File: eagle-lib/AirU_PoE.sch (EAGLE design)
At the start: 86 parts, among them Q1 BSS138W-7-F, Q2 MMBT3904LT1G, Q3 MMBT3904LT1G, Q5 NCE3407A, U1 HDC1080DMBT, U2 CH340T-SSOP20, U3 CJT1117-3.3-SOT223, U4 MAX2659-DFN6, U5 L70-M39, U6 MOLEX-53261-0871, U7 ESP32_WROOM32_SKINNY, U8 TLV2333, U9 MICS-4514, Y1 12MHZ

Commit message: Added PoE components
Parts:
- added C33: 10uf, Seeed-Capacitor:CERAMIC-10UF-10V-10%-X5R(0603)
- added C34, C35: 100nf, Seeed-Capacitor:CERAMIC-100NF-50V-10%-X7R(0603)
- added C36: 33nf, Seeed-Capacitor:CERAMIC-33NF-50V-10%-X7R(0603)
- added D10, D11, D12, D13, D14, D15, D16, D9: 250mA/100V, SparkFun-DiscreteSemi:DIODE-BAS16J
- added J8: SI-52003-F, SI-52003-F:SI-52003-F
- added L4: 330R-1500MA, Seeed-Inductor:SMD-FERRITE-BEAD-330R-1500MA(0805)'0805'
- added R39, R40: 470, SparkFun-Resistors:470OHM-0603-1/10W-1%
- added R41: 2.32k, SparkFun-Resistors:2.2KOHM-0603-1/10W-1%
- added R42, R43, R44, R45: 49.9, BeagleBone_Black_Wireless:R-US_M0805
- added R47: 1K, Seeed-Resistor:SMD-RES-1K-1%-1/10W(0603)
- added U$22: SPXO25MHZ7050-4P, 25MHZ_seeed:SPXO25MHZ7050-4P
- added U10: ENC28J60ENC28J60-I/SS0P, ENC28J60QFN:ENC28J60ENC28J60-I/SS0P
- added U13: AG9900M, AG9900M:AG9900M
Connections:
- removed net SD_CLK_IO14: R15.1, SD1.SCLK, U7.IO14/A2_6
- removed net SD_CMD_IO15: R17.1, SD1.DI, U7.IO15/A2_3
- removed net SD_CS_IO13: R8.1, SD1.CS, U7.IO13/A2_4
- removed net SD_D0_IO2: R12.2, R9.1, SD1.DO, U7.IO2/A2_2
- removed net SD_D1_IO4: SD1.DATA1, U7.IO4/A2_0
- removed net SD_D2_IO12: SD1.DATA2, U7.IO12/A2_5
- new net ETH_LED1: J8.C1, R39.2
- new net ETH_LED2: J8.C2, R40.2
- new net ETH_OSC1: U$22.OUT, U10.OSC1
- new net ETH_OSC2: R47.1, U10.OSC2
- new net ETH_TPIN+: J8.RD+, R43.2, U10.TPIN+
- new net ETH_TPIN-: J8.RD-, R42.1, U10.TPIN-
- new net ETH_TPOUT+: J8.TD+, R45.2, U10.TPOUT+
- new net ETH_TPOUT-: J8.TD-, R44.1, U10.TPOUT-
- new net ETH_VC1+: D10.C, D9.A, J8.VC1+
- new net ETH_VC1-: D15.A, D16.C, J8.VC1-
- new net ETH_VC2+: D11.C, D12.A, J8.VC2+
- new net ETH_VC2-: D13.A, D14.C, J8.VC2-
- new net LEDA: R39.1, U10.LEDA
- new net LEDB: R40.1, U10.LEDB
- new net N$43: C35.2, R42.2, R43.1
- new net N$46: C34.2, J8.CT, L4.1, R44.2, R45.1
- new net PHY_SPI_CS_IO16: U10.!CS, U7.IO16
- new net PHY_SPI_INT_IO25: U10.!INT, U7.IO25/DAC1/A2_8
- new net POE_VIN+: D12.C, D13.C, D15.C, D9.C, U13.VIN+@5, U13.VIN+@6
- new net POE_VIN-: D10.A, D11.A, D14.A, D16.A, U13.VIN-@7, U13.VIN-@8
- new net RBIAS: R41.1, U10.RBIAS
- new net SD_SPI_CS_IO5: R8.1, SD1.CS, U7.IO5
- new net SPI_CLK_IO14: R15.1, SD1.SCLK, U10.SCK, U7.IO14/A2_6
- new net SPI_MISO_IO12: R9.1, SD1.DO, U10.SO, U7.IO12/A2_5
- new net SPI_MOSI_IO15: R17.1, SD1.DI, U10.SI, U7.IO15/A2_3
- new net VCAP: C33.1, U10.VCAP
- net 3.3V: now also C36.1, J8.A1, J8.A2, L4.2, U$22.VCC, U10.VDD, U10.VDDOSC, U10.VDDPLL, U10.VDDRX, U10.VDDTX
- net 5.0V: now also U13.+VDC@1, U13.+VDC@2
- net GND: now also C33.2, C34.1, C35.1, C36.2, J8.S1, J8.S2, R41.2, R47.2, U$22.GND, U10.VSS, U10.VSSOSC, U10.VSSPLL, U10.VSSRX, U10.VSSTX, U13.-VDC
- net PM_RESET: now also R12.2, U7.IO2/A2_2; no longer U7.IO17
- net PM_SET: now also U7.IO4/A2_0; no longer U7.IO5
- net U2RXD: now also U7.IO13/A2_4; no longer U7.IO16
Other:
- note added: "Ethernet PHY"
- note added: "Oscillator (for Ethernet PHY)"
- note added: "Power Over Ethernet (PoE) control"
- note added: "RJ45 Ethernet Jack"

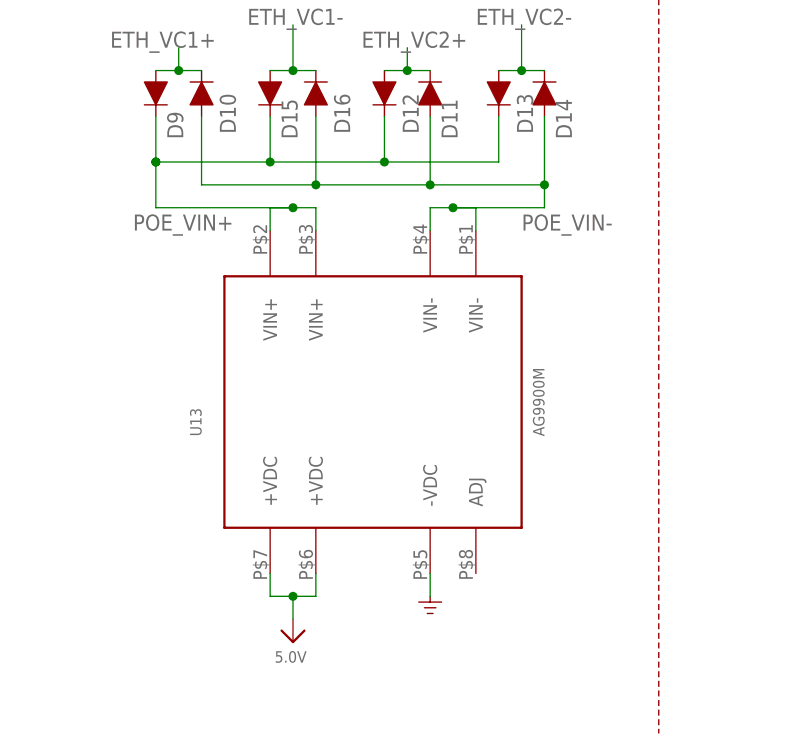
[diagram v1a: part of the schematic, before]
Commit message: fixed AG9900M pins
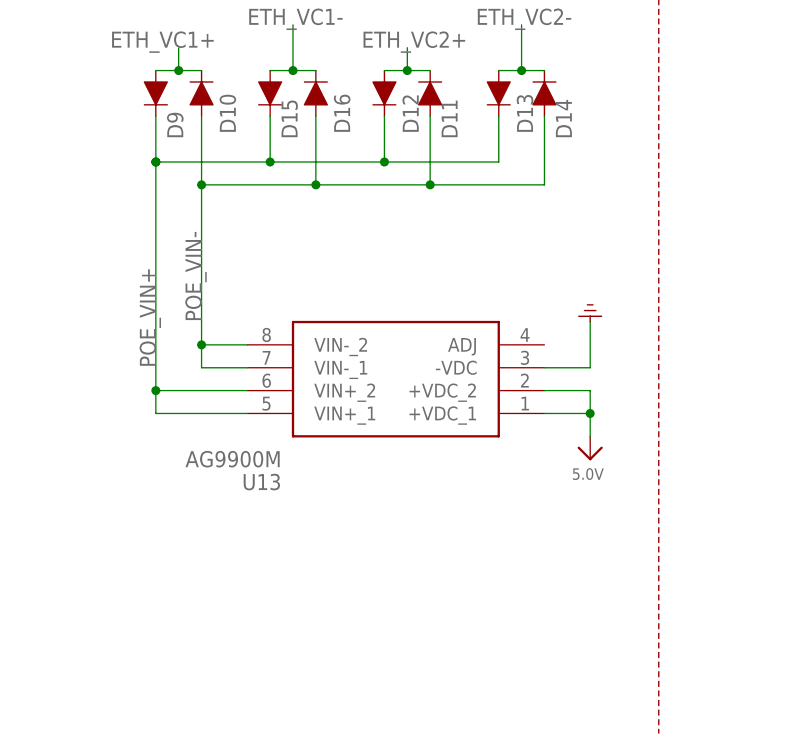
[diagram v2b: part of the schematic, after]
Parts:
- U13: device AG9900M:AG9900M -> Ag9900M:AG9900M
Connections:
- net 5.0V: now also U13.+VDC_1, U13.+VDC_2; no longer U13.+VDC@1, U13.+VDC@2
- net POE_VIN+: now also U13.VIN+_1, U13.VIN+_2; no longer U13.VIN+@5, U13.VIN+@6
- net POE_VIN-: now also U13.VIN-_1, U13.VIN-_2; no longer U13.VIN-@7, U13.VIN-@8
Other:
- moved on the sheet: U13
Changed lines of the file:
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@@
 <part name="U10" library="ENC28J60QFN" deviceset="ENC28J60" device="ENC28J60-I/SS0P" package3d_urn="urn:adsk.eagle:package:11158957/1"/>
 <part name="J8" library="SI-52003-F" deviceset="SI-52003-F" device=""/>
-<part name="U13" library="AG9900M" deviceset="AG9900M" device=""/>
 <part name="FRAME4" library="frames" library_urn="urn:adsk.eagle:library:229" deviceset="FRAME_B_L" device=""/>
 <part name="U$29" library="Power or GND " deviceset="GND_POWER" device=""/>
@@
 <part name="U$22" library="25MHZ_seeed" deviceset="SPXO25MHZ7050-4P" device="" package3d_urn="urn:adsk.eagle:package:14869334/1"/>
 <part name="C36" library="Seeed-Capacitor" deviceset="CERAMIC-33NF-50V-10%-X7R(0603)" device="" value="33nf"/>
+<part name="U13" library="Ag9900M" deviceset="AG9900M" device=""/>
 </parts>
 <sheets>
@@
 <attribute name="VALUE" x="259.065340625" y="55.8458" size="1.78141875" layer="96"/>
 </instance>
-<instance part="U13" gate="G$1" x="43.18" y="38.1" smashed="yes" rot="R90">
-<attribute name="NAME" x="25.4" y="33.02" size="1.27" layer="95" rot="R90"/>
-<attribute name="VALUE" x="63.5" y="33.02" size="1.27" layer="96" rot="R90"/>
-</instance>
 <instance part="FRAME4" gate="G$1" x="0" y="0" smashed="yes"/>
 <instance part="U$29" gate="G$1" x="299.72" y="68.58" smashed="yes" rot="R270"/>
@@
 <attribute name="VALUE" x="158.496" y="128.016" size="1.27" layer="96"/>
 </instance>
-<instance part="U$66" gate="G$1" x="50.8" y="15.24" smashed="yes"/>
+<instance part="U$66" gate="G$1" x="68.58" y="45.72" smashed="yes" rot="R180"/>
 <instance part="U$67" gate="G$1" x="168.91" y="45.72" smashed="yes" rot="R90"/>
 <instance part="U$68" gate="G$1" x="168.91" y="58.42" smashed="yes" rot="R90"/>
@@
 <attribute name="VALUE" x="103.124" y="72.136" size="1.27" layer="96" rot="R90"/>
 </instance>
-<instance part="U$94" gate="G$1" x="35.56" y="10.16" smashed="yes" rot="R180">
-<attribute name="VALUE" x="37.084" y="9.144" size="1.27" layer="96" rot="R180"/>
+<instance part="U$94" gate="G$1" x="68.58" y="30.48" smashed="yes" rot="R180">
+<attribute name="VALUE" x="70.104" y="29.464" size="1.27" layer="96" rot="R180"/>
 </instance>
 <instance part="U$1" gate="G$1" x="218.44" y="78.74" smashed="yes">
@@
 <attribute name="NAME" x="326.39" y="45.72" size="1.27" layer="95" ratio="10" rot="R180"/>
 <attribute name="VALUE" x="326.39" y="49.53" size="1.27" layer="96" ratio="10" rot="R180"/>
+</instance>
+<instance part="U13" gate="G$1" x="63.5" y="35.56" smashed="yes" rot="R180">
+<attribute name="NAME" x="34.29" y="27.94" size="1.778" layer="95" rot="R180" align="center-left"/>
+<attribute name="VALUE" x="34.29" y="30.48" size="1.778" layer="96" rot="R180" align="center-left"/>
 </instance>
 </instances>
@@
 </segment>
 <segment>
-<pinref part="U13" gate="G$1" pin="-VDC"/>
-<wire x1="50.8" y1="17.78" x2="50.8" y2="15.24" width="0.1524" layer="91"/>
-<pinref part="U$66" gate="G$1" pin="GND"/>
-</segment>
-<segment>
 <pinref part="J8" gate="G$1" pin="S1"/>
 <wire x1="261.62" y1="15.24" x2="261.62" y2="12.7" width="0.1524" layer="91"/>
@@
 <pinref part="C33" gate="G$1" pin="2"/>
 <wire x1="95.25" y1="33.02" x2="100.33" y2="33.02" width="0.1524" layer="91"/>
+</segment>
+<segment>
+<pinref part="U13" gate="G$1" pin="-VDC"/>
+<pinref part="U$66" gate="G$1" pin="GND"/>
+<wire x1="63.5" y1="40.64" x2="68.58" y2="40.64" width="0.1524" layer="91"/>
+<wire x1="68.58" y1="40.64" x2="68.58" y2="45.72" width="0.1524" layer="91"/>
 </segment>
 </net>
@@
 </segment>
 <segment>
-<pinref part="U13" gate="G$1" pin="+VDC@1"/>
-<wire x1="33.02" y1="17.78" x2="33.02" y2="15.24" width="0.1524" layer="91"/>
+<pinref part="U13" gate="G$1" pin="+VDC_2"/>
 <pinref part="U$94" gate="G$1" pin="5.0V"/>
-<wire x1="33.02" y1="15.24" x2="35.56" y2="15.24" width="0.1524" layer="91"/>
-<wire x1="35.56" y1="15.24" x2="35.56" y2="12.7" width="0.1524" layer="91"/>
-<pinref part="U13" gate="G$1" pin="+VDC@2"/>
-<wire x1="38.1" y1="15.24" x2="38.1" y2="17.78" width="0.1524" layer="91"/>
-<wire x1="38.1" y1="15.24" x2="35.56" y2="15.24" width="0.1524" layer="91"/>
-<junction x="35.56" y="15.24"/>
+<wire x1="63.5" y1="38.1" x2="68.58" y2="38.1" width="0.1524" layer="91"/>
+<wire x1="68.58" y1="38.1" x2="68.58" y2="35.56" width="0.1524" layer="91"/>
+<pinref part="U13" gate="G$1" pin="+VDC_1"/>
+<wire x1="68.58" y1="35.56" x2="68.58" y2="33.02" width="0.1524" layer="91"/>
+<wire x1="63.5" y1="35.56" x2="68.58" y2="35.56" width="0.1524" layer="91"/>
+<junction x="68.58" y="35.56"/>
 </segment>
 </net>
@@
 <wire x1="50.8" y1="60.96" x2="63.5" y2="60.96" width="0.1524" layer="91"/>
 <pinref part="D11" gate="G$1" pin="A"/>
-<wire x1="63.5" y1="60.96" x2="63.5" y2="58.42" width="0.1524" layer="91"/>
-<pinref part="U13" gate="G$1" pin="VIN-@7"/>
-<wire x1="50.8" y1="55.88" x2="50.8" y2="58.42" width="0.1524" layer="91"/>
-<wire x1="50.8" y1="58.42" x2="53.34" y2="58.42" width="0.1524" layer="91"/>
-<pinref part="U13" gate="G$1" pin="VIN-@8"/>
-<wire x1="53.34" y1="58.42" x2="55.88" y2="58.42" width="0.1524" layer="91"/>
-<wire x1="55.88" y1="58.42" x2="55.88" y2="55.88" width="0.1524" layer="91"/>
-<wire x1="63.5" y1="58.42" x2="53.34" y2="58.42" width="0.1524" layer="91"/>
-<junction x="53.34" y="58.42"/>
 <wire x1="38.1" y1="60.96" x2="38.1" y2="68.58" width="0.1524" layer="91"/>
 <junction x="38.1" y="60.96"/>
@@
 <junction x="50.8" y="60.96"/>
 <wire x1="63.5" y1="60.96" x2="63.5" y2="68.58" width="0.1524" layer="91"/>
-<junction x="63.5" y="60.96"/>
-<label x="60.96" y="55.88" size="1.778" layer="95"/>
+<label x="25.4" y="45.72" size="1.778" layer="95" rot="R90"/>
+<pinref part="U13" gate="G$1" pin="VIN-_1"/>
+<wire x1="25.4" y1="60.96" x2="25.4" y2="43.18" width="0.1524" layer="91"/>
+<wire x1="25.4" y1="43.18" x2="25.4" y2="40.64" width="0.1524" layer="91"/>
+<wire x1="25.4" y1="40.64" x2="30.48" y2="40.64" width="0.1524" layer="91"/>
+<junction x="25.4" y="60.96"/>
+<pinref part="U13" gate="G$1" pin="VIN-_2"/>
+<wire x1="30.48" y1="43.18" x2="25.4" y2="43.18" width="0.1524" layer="91"/>
+<junction x="25.4" y="43.18"/>
 </segment>
 </net>
@@
 <wire x1="20.32" y1="68.58" x2="20.32" y2="63.5" width="0.1524" layer="91"/>
 <junction x="20.32" y="63.5"/>
-<wire x1="20.32" y1="63.5" x2="20.32" y2="58.42" width="0.1524" layer="91"/>
-<wire x1="20.32" y1="58.42" x2="35.56" y2="58.42" width="0.1524" layer="91"/>
-<pinref part="U13" gate="G$1" pin="VIN+@5"/>
-<wire x1="33.02" y1="55.88" x2="33.02" y2="58.42" width="0.1524" layer="91"/>
-<wire x1="33.02" y1="58.42" x2="35.56" y2="58.42" width="0.1524" layer="91"/>
-<pinref part="U13" gate="G$1" pin="VIN+@6"/>
-<wire x1="38.1" y1="55.88" x2="38.1" y2="58.42" width="0.1524" layer="91"/>
-<wire x1="38.1" y1="58.42" x2="35.56" y2="58.42" width="0.1524" layer="91"/>
-<junction x="35.56" y="58.42"/>
 <wire x1="33.02" y1="63.5" x2="20.32" y2="63.5" width="0.1524" layer="91"/>
 <junction x="20.32" y="63.5"/>
@@
 <wire x1="45.72" y1="63.5" x2="58.42" y2="63.5" width="0.1524" layer="91"/>
 <wire x1="58.42" y1="63.5" x2="58.42" y2="68.58" width="0.1524" layer="91"/>
-<label x="17.78" y="55.88" size="1.778" layer="95"/>
-</segment>
-</net>
+<label x="20.32" y="40.64" size="1.778" layer="95" rot="R90"/>
+<wire x1="20.32" y1="63.5" x2="20.32" y2="38.1" width="0.1524" layer="91"/>
+<pinref part="U13" gate="G$1" pin="VIN+_1"/>
+<wire x1="20.32" y1="38.1" x2="20.32" y2="35.56" width="0.1524" layer="91"/>
+<wire x1="20.32" y1="35.56" x2="30.48" y2="35.56" width="0.1524" layer="91"/>
+<pinref part="U13" gate="G$1" pin="VIN+_2"/>
+<wire x1="20.32" y1="38.1" x2="30.48" y2="38.1" width="0.1524" layer="91"/>
+<junction x="20.32" y="38.1"/>
+</segment>
+</net>
